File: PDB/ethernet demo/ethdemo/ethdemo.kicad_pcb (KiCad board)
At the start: 4 copper layers, 77.5 x 67.5 mm, 99 parts, among them J1 0826-1X1T-GJ-F, J2 0826-1X1T-GJ-F, J3 Conn_01x05_Socket, Q1 CSD19538Q3AT, U1 STM32H742VGTx, U2 KSZ8863RLLI, U3 TPS23861PWR, Y1 25MHz

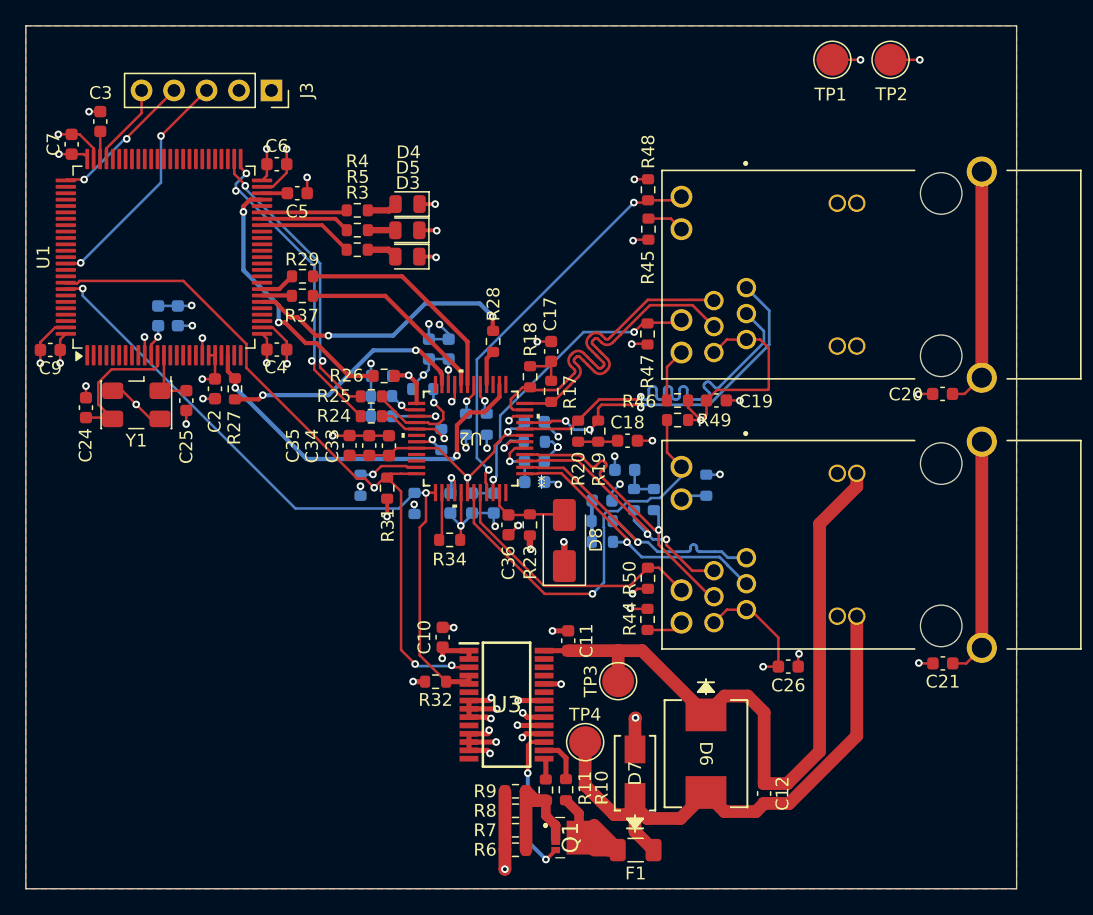
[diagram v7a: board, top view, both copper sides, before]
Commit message: added production files and one edit
removed GND poor accidently made on top layer since it was all disconnected
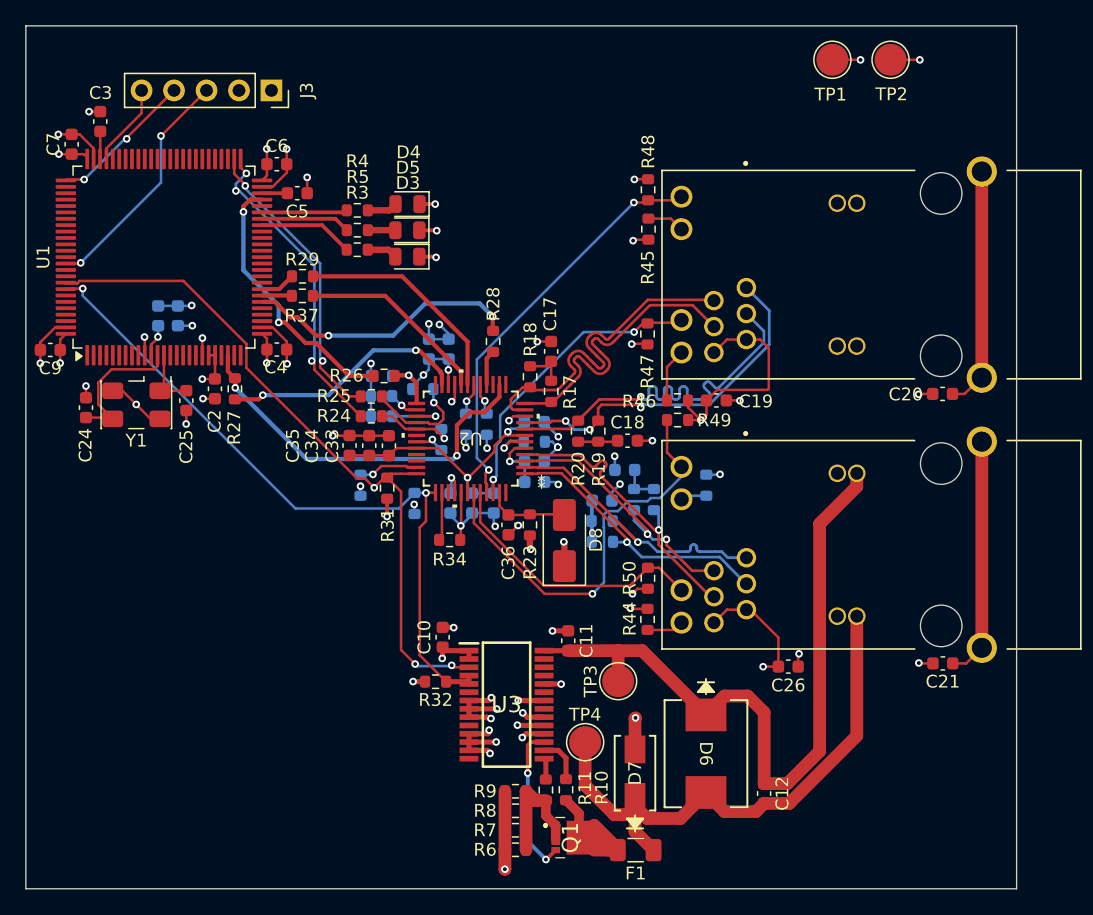
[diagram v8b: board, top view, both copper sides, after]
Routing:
- removed copper zone on F.Cu, net GND
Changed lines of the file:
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@@
+	)
+	(segment
+		(start 188.3 65.7325)
+		(end 187.99 66.0425)
+		(width 0.2)
+		(layer "F.Cu")
+		(net "/OCS1")
+	)
+	(segment
+		(start 188.3 63.265)
+		(end 188.3 65.7325)
+		(width 0.2)
+		(layer "F.Cu")
+		(net "/OCS1")
+	)
+	(segment
+		(start 187.99 66.0425)
+		(end 190.0425 66.0425)
+		(width 0.2)
+		(layer "F.Cu")
+		(net "/OCS1")
+	)
+	(segment
+		(start 187.99 66.0425)
+		(end 187.8 65.8525)
+		(width 0.2)
+		(layer "F.Cu")
+		(net "/OCS1")
+	)
+	(segment
+		(start 190.0425 66.0425)
+		(end 190.05 66.035)
+		(width 0.2)
+		(layer "F.Cu")
+		(net "/OCS1")
 	)
 	(segment
@@
 	)
 	(segment
+		(start 181.737172 56.09)
+		(end 180.625 56.09)
+		(width 0.2)
+		(layer "F.Cu")
+		(net "/SWO{slash}TRACE")
+	)
+	(segment
+		(start 191.63 42.55)
+		(end 188.07 46.11)
+		(width 0.2)
+		(layer "F.Cu")
+		(net "/SWO{slash}TRACE")
+	)
+	(segment
+		(start 181.789044 56.038128)
+		(end 181.737172 56.09)
+		(width 0.2)
+		(layer "F.Cu")
+		(net "/SWO{slash}TRACE")
+	)
+	(via
+		(at 181.789044 56.038128)
+		(size 0.6)
+		(drill 0.3)
+		(layers "F.Cu" "B.Cu")
+		(net "/SWO{slash}TRACE")
+	)
+	(via
+		(at 188.07 46.11)
+		(size 0.6)
+		(drill 0.3)
+		(layers "F.Cu" "B.Cu")
+		(net "/SWO{slash}TRACE")
+	)
+	(segment
+		(start 188.07 49.757172)
+		(end 181.789044 56.038128)
+		(width 0.2)
+		(layer "B.Cu")
+		(net "/SWO{slash}TRACE")
+	)
+	(segment
+		(start 188.07 46.11)
+		(end 188.07 49.757172)
+		(width 0.2)
+		(layer "B.Cu")
+		(net "/SWO{slash}TRACE")
+	)
+	(segment
+		(start 182.06 49.52)
+		(end 180.695 49.52)
+		(width 0.2)
+		(layer "F.Cu")
+		(net "/SWCLK")
+	)
+	(segment
+		(start 180.695 49.52)
+		(end 180.625 49.59)
+		(width 0.2)
+		(layer "F.Cu")
+		(net "/SWCLK")
+	)
+	(segment
+		(start 185.39056 46.24944)
+		(end 185.39056 46.34056)
+		(width 0.2)
+		(layer "F.Cu")
+		(net "/SWCLK")
+	)
+	(segment
+		(start 189.09 42.55)
+		(end 185.39056 46.24944)
+		(width 0.2)
+		(layer "F.Cu")
+		(net "/SWCLK")
+	)
+	(via
+		(at 185.39056 46.34056)
+		(size 0.6)
+		(drill 0.3)
+		(layers "F.Cu" "B.Cu")
+		(net "/SWCLK")
+	)
+	(via
+		(at 182.06 49.52)
+		(size 0.6)
+		(drill 0.3)
+		(layers "F.Cu" "B.Cu")
+		(net "/SWCLK")
+	)
+	(segment
+		(start 185.39056 46.34056)
+		(end 185.23944 46.34056)
+		(width 0.2)
+		(layer "B.Cu")
+		(net "/SWCLK")
+	)
+	(segment
+		(start 185.23944 46.34056)
+		(end 182.06 49.52)
+		(width 0.2)
+		(layer "B.Cu")
+		(net "/SWCLK")
+	)
+	(segment
+		(start 186.55 42.55)
+		(end 186.55 44.33259)
+		(width 0.2)
+		(layer "F.Cu")
+		(net "/SWDIO")
+	)
+	(segment
+		(start 183.8 47.08259)
+		(end 183.8 47.915)
+		(width 0.2)
+		(layer "F.Cu")
+		(net "/SWDIO")
+	)
+	(segment
+		(start 186.55 44.33259)
+		(end 183.8 47.08259)
+		(width 0.2)
+		(layer "F.Cu")
+		(net "/SWDIO")
+	)
+	(segment
 		(start 205.8625 55.01)
 		(end 206.4025 55.55)
@@
 	)
 	(segment
-		(start 188.3 65.7325)
-		(end 187.99 66.0425)
-		(width 0.2)
-		(layer "F.Cu")
-		(net "/OCS1")
-	)
-	(segment
-		(start 188.3 63.265)
-		(end 188.3 65.7325)
-		(width 0.2)
-		(layer "F.Cu")
-		(net "/OCS1")
-	)
-	(segment
-		(start 187.99 66.0425)
-		(end 190.0425 66.0425)
-		(width 0.2)
-		(layer "F.Cu")
-		(net "/OCS1")
-	)
-	(segment
-		(start 187.99 66.0425)
-		(end 187.8 65.8525)
-		(width 0.2)
-		(layer "F.Cu")
-		(net "/OCS1")
-	)
-	(segment
-		(start 190.0425 66.0425)
-		(end 190.05 66.035)
-		(width 0.2)
-		(layer "F.Cu")
-		(net "/OCS1")
-	)
-	(segment
 		(start 200.195686 61.73)
 		(end 198.768085 60.302399)
@@
 	)
 	(segment
-		(start 186.55 42.55)
-		(end 186.55 44.33259)
-		(width 0.2)
-		(layer "F.Cu")
-		(net "/SWDIO")
-	)
-	(segment
-		(start 183.8 47.08259)
-		(end 183.8 47.915)
-		(width 0.2)
-		(layer "F.Cu")
-		(net "/SWDIO")
-	)
-	(segment
-		(start 186.55 44.33259)
-		(end 183.8 47.08259)
-		(width 0.2)
-		(layer "F.Cu")
-		(net "/SWDIO")
-	)
-	(segment
-		(start 182.06 49.52)
-		(end 180.695 49.52)
-		(width 0.2)
-		(layer "F.Cu")
-		(net "/SWCLK")
-	)
-	(segment
-		(start 180.695 49.52)
-		(end 180.625 49.59)
-		(width 0.2)
-		(layer "F.Cu")
-		(net "/SWCLK")
-	)
-	(segment
-		(start 185.39056 46.24944)
-		(end 185.39056 46.34056)
-		(width 0.2)
-		(layer "F.Cu")
-		(net "/SWCLK")
-	)
-	(segment
-		(start 189.09 42.55)
-		(end 185.39056 46.24944)
-		(width 0.2)
-		(layer "F.Cu")
-		(net "/SWCLK")
-	)
-	(via
-		(at 185.39056 46.34056)
-		(size 0.6)
-		(drill 0.3)
-		(layers "F.Cu" "B.Cu")
-		(net "/SWCLK")
-	)
-	(via
-		(at 182.06 49.52)
-		(size 0.6)
-		(drill 0.3)
-		(layers "F.Cu" "B.Cu")
-		(net "/SWCLK")
-	)
-	(segment
-		(start 185.39056 46.34056)
-		(end 185.23944 46.34056)
-		(width 0.2)
-		(layer "B.Cu")
-		(net "/SWCLK")
-	)
-	(segment
-		(start 185.23944 46.34056)
-		(end 182.06 49.52)
-		(width 0.2)
-		(layer "B.Cu")
-		(net "/SWCLK")
-	)
-	(segment
-		(start 181.737172 56.09)
-		(end 180.625 56.09)
-		(width 0.2)
-		(layer "F.Cu")
-		(net "/SWO{slash}TRACE")
-	)
-	(segment
-		(start 191.63 42.55)
-		(end 188.07 46.11)
-		(width 0.2)
-		(layer "F.Cu")
-		(net "/SWO{slash}TRACE")
-	)
-	(segment
-		(start 181.789044 56.038128)
-		(end 181.737172 56.09)
-		(width 0.2)
-		(layer "F.Cu")
-		(net "/SWO{slash}TRACE")
-	)
-	(via
-		(at 181.789044 56.038128)
-		(size 0.6)
-		(drill 0.3)
-		(layers "F.Cu" "B.Cu")
-		(net "/SWO{slash}TRACE")
-	)
-	(via
-		(at 188.07 46.11)
-		(size 0.6)
-		(drill 0.3)
-		(layers "F.Cu" "B.Cu")
-		(net "/SWO{slash}TRACE")
-	)
-	(segment
-		(start 188.07 49.757172)
-		(end 181.789044 56.038128)
-		(width 0.2)
-		(layer "B.Cu")
-		(net "/SWO{slash}TRACE")
-	)
-	(segment
-		(start 188.07 46.11)
-		(end 188.07 49.757172)
-		(width 0.2)
-		(layer "B.Cu")
-		(net "/SWO{slash}TRACE")
-	)
-	(segment
 		(start 221.775 74.658347)
 		(end 221.8 74.633347)
@@
 	)
 	(zone
-		(net "GND")
-		(layer "F.Cu")
-		(hatch edge 0.5)
-		(priority 2)
-		(connect_pads
-			(clearance 4.786)
-		)
-		(min_thickness 0.25)
-		(fill
-			(thermal_gap 0.5)
-			(thermal_bridge_width 0.5)
-			(island_removal_mode 0)
-		)
-		(polygon
-			(pts
-				(xy 177.5 37.5) (xy 255 37.5) (xy 255 105) (xy 177.5 105)
-			)
-		)
-	)
-	(zone
